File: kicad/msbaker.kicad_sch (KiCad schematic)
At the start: 27 parts

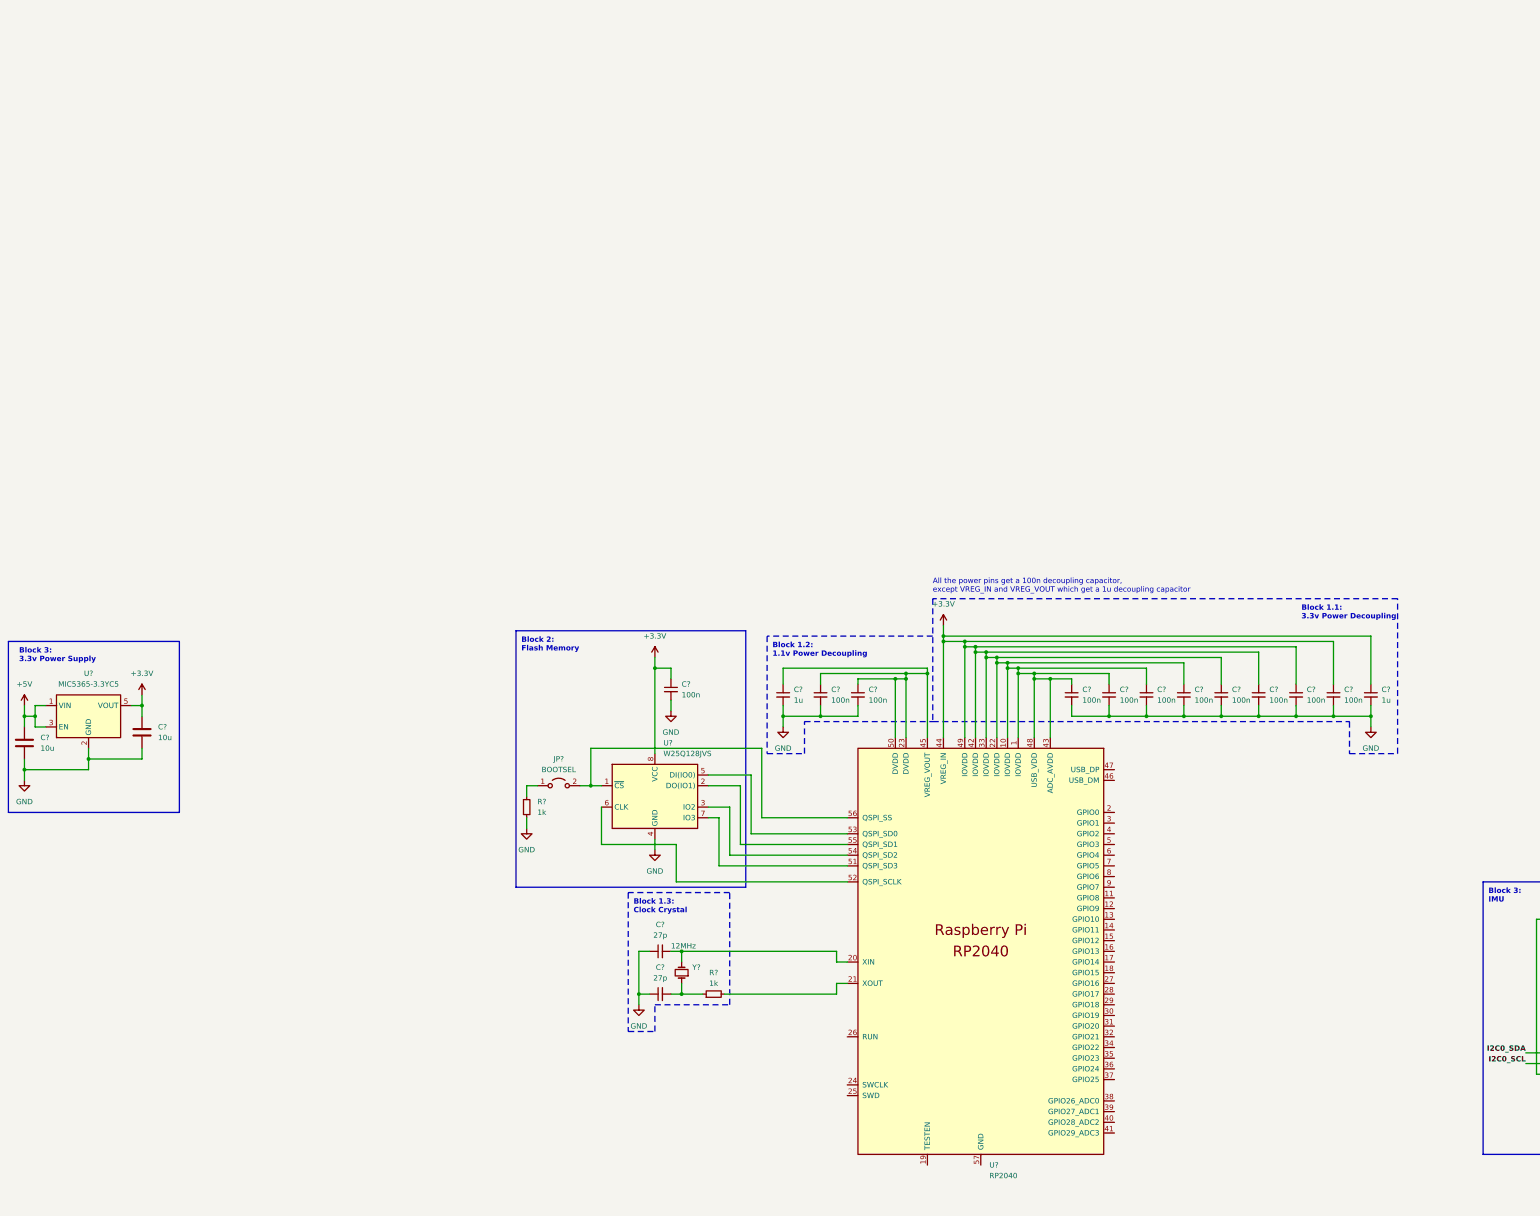
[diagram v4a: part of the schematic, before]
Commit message: Added USB block
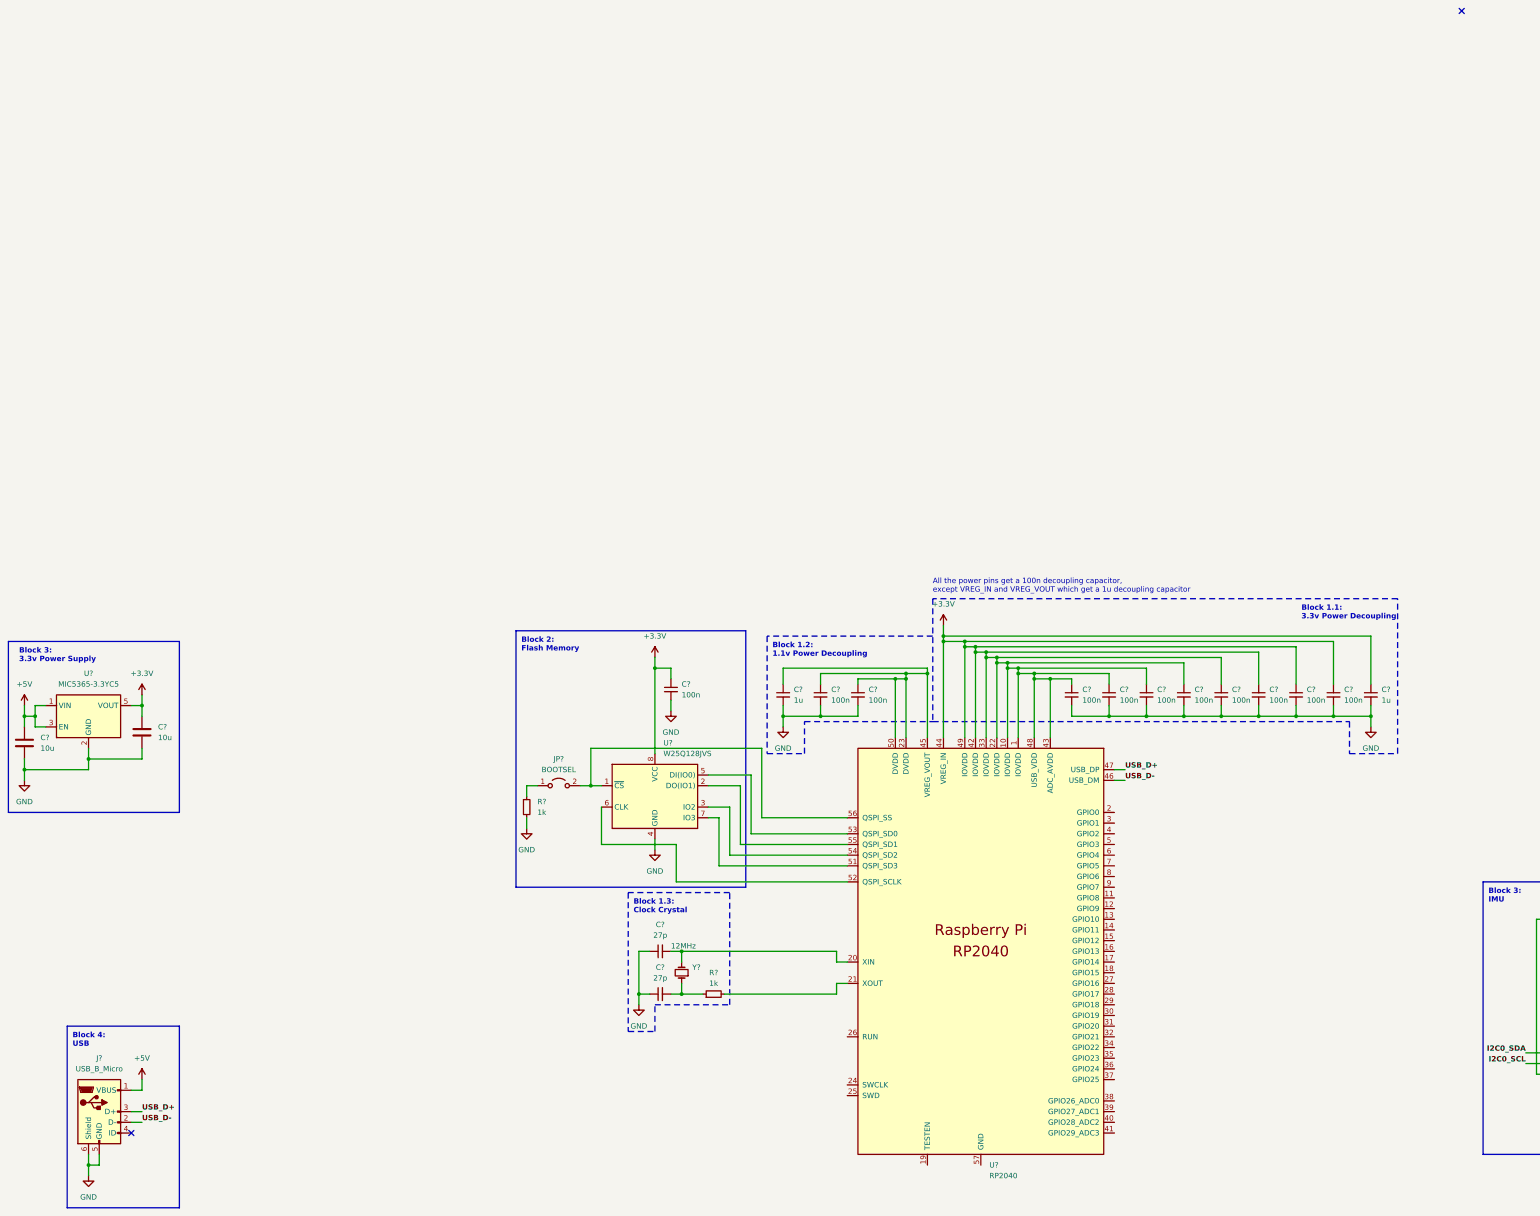
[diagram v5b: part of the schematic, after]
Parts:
- added J?: USB_B_Micro, symbol Connector:USB_B_Micro
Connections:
- net +5V: now also J?.1 (VBUS)
- net GND: now also J?.5 (GND), J?.6 (Shield)
- net USB_D-: now reaches U?.46 (USB_DM)
- net USB_D-: now also J?.2 (D-)
- net USB_D+: now reaches U?.47 (USB_DP)
- net USB_D+: now also J?.3 (D+)
- no-connect marks 2 -> 4
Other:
- note added: "Block 4: USB"
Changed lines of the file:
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@@
     (rev "3")
   )
+  (junction (at 121.92 276.86) (diameter 0) (color 0 0 0 0)
+  )
   (junction (at 486.41 265.43) (diameter 0) (color 0 0 0 0)
   )
@@
   (junction (at 337.82 156.21) (diameter 0) (color 0 0 0 0)
   )
+  (no_connect (at 448.31 2.54))
+  (no_connect (at 132.08 269.24))
   (no_connect (at 501.65 240.03))
   (no_connect (at 501.65 242.57))
@@
     (stroke (width 0) (type default) (color 0 0 0 0))
   )
+  (wire (pts (xy 132.08 266.7) (xy 134.62 266.7))
+    (stroke (width 0) (type default) (color 0 0 0 0))
+  )
   (wire (pts (xy 295.91 160.02) (xy 295.91 162.56))
     (stroke (width 0) (type default) (color 0 0 0 0))
@@
     (stroke (width 0) (type default) (color 0 0 0 0))
   )
+  (wire (pts (xy 124.46 274.32) (xy 124.46 276.86))
+    (stroke (width 0) (type default) (color 0 0 0 0))
+  )
   (wire (pts (xy 256.54 199.39) (xy 256.54 201.93))
     (stroke (width 0) (type default) (color 0 0 0 0))
@@
   )
   (wire (pts (xy 299.72 228.6) (xy 302.26 228.6))
+    (stroke (width 0) (type default) (color 0 0 0 0))
+  )
+  (wire (pts (xy 132.08 259.08) (xy 134.62 259.08))
     (stroke (width 0) (type default) (color 0 0 0 0))
   )
@@
     (stroke (width 0) (type default) (color 0 0 0 0))
   )
+  (polyline (pts (xy 116.84 287.02) (xy 143.51 287.02))
+    (stroke (width 0) (type default) (color 0 0 0 0))
+  )
   (polyline (pts (xy 274.32 238.76) (xy 274.32 212.09))
     (stroke (width 0) (type dot) (color 0 0 0 0))
   )
+  (wire (pts (xy 121.92 274.32) (xy 121.92 276.86))
+    (stroke (width 0) (type default) (color 0 0 0 0))
+  )
   (polyline (pts (xy 223.52 149.86) (xy 278.13 149.86))
     (stroke (width 0) (type default) (color 0 0 0 0))
@@
     (stroke (width 0) (type default) (color 0 0 0 0))
   )
+  (wire (pts (xy 121.92 276.86) (xy 121.92 279.4))
+    (stroke (width 0) (type default) (color 0 0 0 0))
+  )
   (wire (pts (xy 382.27 170.18) (xy 391.16 170.18))
     (stroke (width 0) (type default) (color 0 0 0 0))
@@
     (stroke (width 0) (type default) (color 0 0 0 0))
   )
+  (polyline (pts (xy 116.84 243.84) (xy 143.51 243.84))
+    (stroke (width 0) (type default) (color 0 0 0 0))
+  )
   (wire (pts (xy 335.28 154.94) (xy 400.05 154.94))
+    (stroke (width 0) (type default) (color 0 0 0 0))
+  )
+  (wire (pts (xy 134.62 259.08) (xy 134.62 256.54))
     (stroke (width 0) (type default) (color 0 0 0 0))
   )
@@
     (stroke (width 0) (type default) (color 0 0 0 0))
   )
+  (polyline (pts (xy 143.51 287.02) (xy 143.51 243.84))
+    (stroke (width 0) (type default) (color 0 0 0 0))
+  )
   (wire (pts (xy 316.23 160.02) (xy 321.31 160.02))
+    (stroke (width 0) (type default) (color 0 0 0 0))
+  )
+  (polyline (pts (xy 116.84 243.84) (xy 116.84 287.02))
     (stroke (width 0) (type default) (color 0 0 0 0))
   )
@@
     (stroke (width 0) (type default) (color 0 0 0 0))
   )
+  (wire (pts (xy 365.76 185.42) (xy 368.3 185.42))
+    (stroke (width 0) (type default) (color 0 0 0 0))
+  )
   (wire (pts (xy 299.72 226.06) (xy 299.72 228.6))
     (stroke (width 0) (type default) (color 0 0 0 0))
@@
   )
   (wire (pts (xy 281.94 194.31) (xy 302.26 194.31))
+    (stroke (width 0) (type default) (color 0 0 0 0))
+  )
+  (wire (pts (xy 132.08 264.16) (xy 134.62 264.16))
     (stroke (width 0) (type default) (color 0 0 0 0))
   )
@@
     (stroke (width 0) (type default) (color 0 0 0 0))
   )
+  (wire (pts (xy 365.76 182.88) (xy 368.3 182.88))
+    (stroke (width 0) (type default) (color 0 0 0 0))
+  )
   (wire (pts (xy 346.71 161.29) (xy 350.52 161.29))
     (stroke (width 0) (type default) (color 0 0 0 0))
@@
   )
   (wire (pts (xy 241.3 186.69) (xy 243.84 186.69))
+    (stroke (width 0) (type default) (color 0 0 0 0))
+  )
+  (wire (pts (xy 124.46 276.86) (xy 121.92 276.86))
     (stroke (width 0) (type default) (color 0 0 0 0))
   )
@@
   )
   (text "Block 3:\n3.3v Power Supply" (at 105.41 157.48 0)
+    (effects (font (size 1.27 1.27) bold) (justify left bottom))
+  )
+  (text "Block 4:\nUSB" (at 118.11 248.92 0)
     (effects (font (size 1.27 1.27) bold) (justify left bottom))
   )
@@
     (effects (font (size 1.27 1.27) bold) (justify right bottom))
   )
+  (label "USB_D+" (at 368.3 182.88 0)
+    (effects (font (size 1.27 1.27) bold) (justify left bottom))
+  )
   (label "I2C0_SDA" (at 463.55 250.19 180)
     (effects (font (size 1.27 1.27) bold) (justify right bottom))
+  )
+  (label "USB_D-" (at 134.62 266.7 0)
+    (effects (font (size 1.27 1.27) bold) (justify left bottom))
+  )
+  (label "USB_D-" (at 368.3 185.42 0)
+    (effects (font (size 1.27 1.27) bold) (justify left bottom))
+  )
+  (label "USB_D+" (at 134.62 264.16 0)
+    (effects (font (size 1.27 1.27) bold) (justify left bottom))
   )
   (symbol (lib_id "Memory_Flash:W25Q128JVS") (at 256.54 189.23 0) (unit 1)
@@
     (pin "1")
   )
+  (symbol (lib_id "Connector:USB_B_Micro") (at 124.46 264.16 0) (unit 1)
+    (in_bom yes) (on_board yes) (fields_autoplaced)
+    (property "Reference" "J?" (id 0) (at 124.46 251.46 0))
+    (property "Value" "USB_B_Micro" (id 1) (at 124.46 254 0))
+    (property "Footprint" "" (id 2) (at 128.27 265.43 0)
+      (effects (font (size 1.27 1.27)) hide)
+    )
+    (property "Datasheet" "~" (id 3) (at 128.27 265.43 0)
+      (effects (font (size 1.27 1.27)) hide)
+    )
+    (pin "1")
+    (pin "2")
+    (pin "3")
+    (pin "4")
+    (pin "5")
+    (pin "6")
+  )
   (symbol (lib_id "power:GND") (at 486.41 267.97 0) (unit 1)
     (in_bom yes) (on_board yes) (fields_autoplaced)
@@
     (pin "1")
     (pin "2")
+  )
+  (symbol (lib_id "power:+5V") (at 134.62 256.54 0) (unit 1)
+    (in_bom yes) (on_board yes) (fields_autoplaced)
+    (property "Reference" "#PWR?" (id 0) (at 134.62 260.35 0)
+      (effects (font (size 1.27 1.27)) hide)
+    )
+    (property "Value" "+5V" (id 1) (at 134.62 251.46 0))
+    (property "Footprint" "" (id 2) (at 134.62 256.54 0)
+      (effects (font (size 1.27 1.27)) hide)
+    )
+    (property "Datasheet" "" (id 3) (at 134.62 256.54 0)
+      (effects (font (size 1.27 1.27)) hide)
+    )
+    (pin "1")
   )
   (symbol (lib_id "Sensor_Motion:LSM6DS3") (at 486.41 247.65 0) (unit 1)
@@
     (pin "2")
   )
+  (symbol (lib_id "power:GND") (at 121.92 279.4 0) (unit 1)
+    (in_bom yes) (on_board yes) (fields_autoplaced)
+    (property "Reference" "#PWR?" (id 0) (at 121.92 285.75 0)
+      (effects (font (size 1.27 1.27)) hide)
+    )
+    (property "Value" "GND" (id 1) (at 121.92 284.48 0))
+    (property "Footprint" "" (id 2) (at 121.92 279.4 0)
+      (effects (font (size 1.27 1.27)) hide)
+    )
+    (property "Datasheet" "" (id 3) (at 121.92 279.4 0)
+      (effects (font (size 1.27 1.27)) hide)
+    )
+    (pin "1")
+  )
   (symbol (lib_id "power:GND") (at 226.06 196.85 0) (unit 1)
     (in_bom yes) (on_board yes) (fields_autoplaced)
@@
       (reference "#PWR?") (unit 1) (value "GND") (footprint "")
     )
+    (path "/9884452c-d9a0-4c8b-8cf5-ccc0fd50b27c"
+      (reference "#PWR?") (unit 1) (value "+5V") (footprint "")
+    )
     (path "/b0238046-43da-4134-9d74-c0e87d0911ba"
       (reference "#PWR?") (unit 1) (value "+3.3V") (footprint "")
@@
       (reference "#PWR?") (unit 1) (value "GND") (footprint "")
     )
+    (path "/f0647cc5-fd08-4417-8baa-f51d945b8021"
+      (reference "#PWR?") (unit 1) (value "GND") (footprint "")
+    )
     (path "/fb46e138-05c5-4456-8aba-b6a7b33ec634"
       (reference "#PWR?") (unit 1) (value "GND") (footprint "")
@@
       (reference "C?") (unit 1) (value "100n") (footprint "")
     )
+    (path "/5b54e395-bfd0-4185-8b8e-958e5c56e676"
+      (reference "J?") (unit 1) (value "USB_B_Micro") (footprint "")
+    )
     (path "/90b3348e-fcba-4fd2-9091-bd5f7ceeabe7"
